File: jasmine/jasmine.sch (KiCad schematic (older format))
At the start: 74 parts, among them J1 NEIGHBOR1, J2 NEIGHBOR2, J3 USB-MICRO-B-SHIELDED, J4 LIPO_BATT_CONN, J5 2PIN_BATT_CONN, J7 BONUS_ROW, P1 TEST_POINT, P2 TEST_POINT, P3 INPUT, P4 3.7_VDC, P5 3.7_VDC, SW1 SW_SPDT, U1 MCP73831T, U2 74HC4051, U3 74HC4051, U4 PCA9674, X1 SiT1533

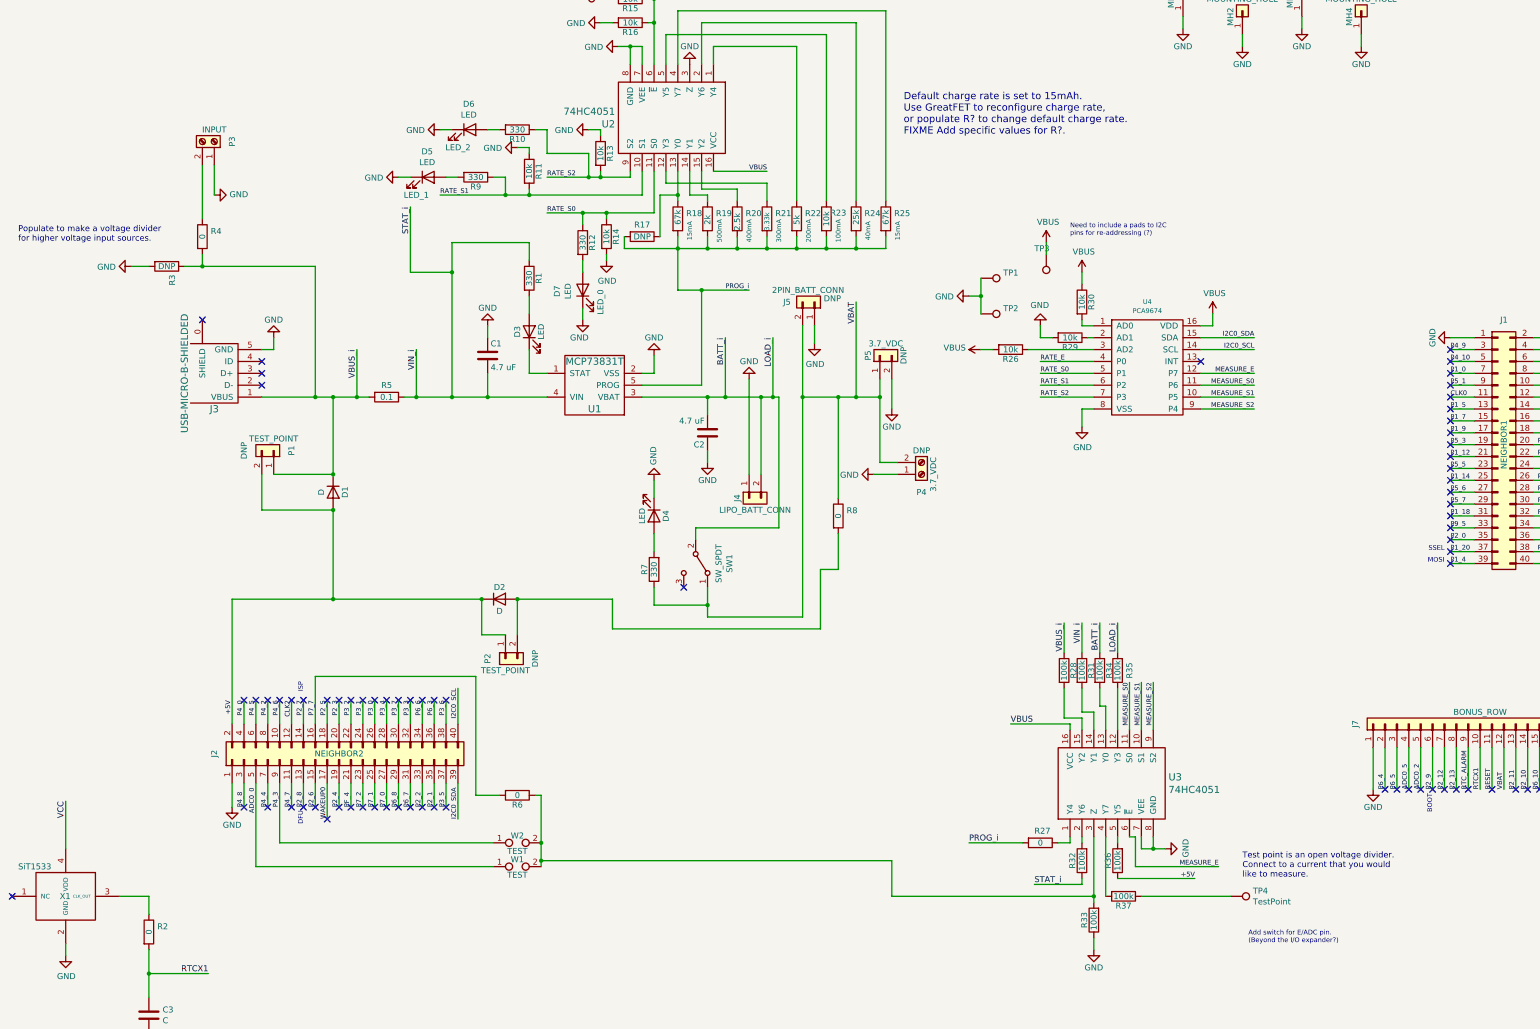
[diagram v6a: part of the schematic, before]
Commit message: Updates to jasmine schematic and layout; Updated neighbor-template to be compatible with KiCAD 5.1.2
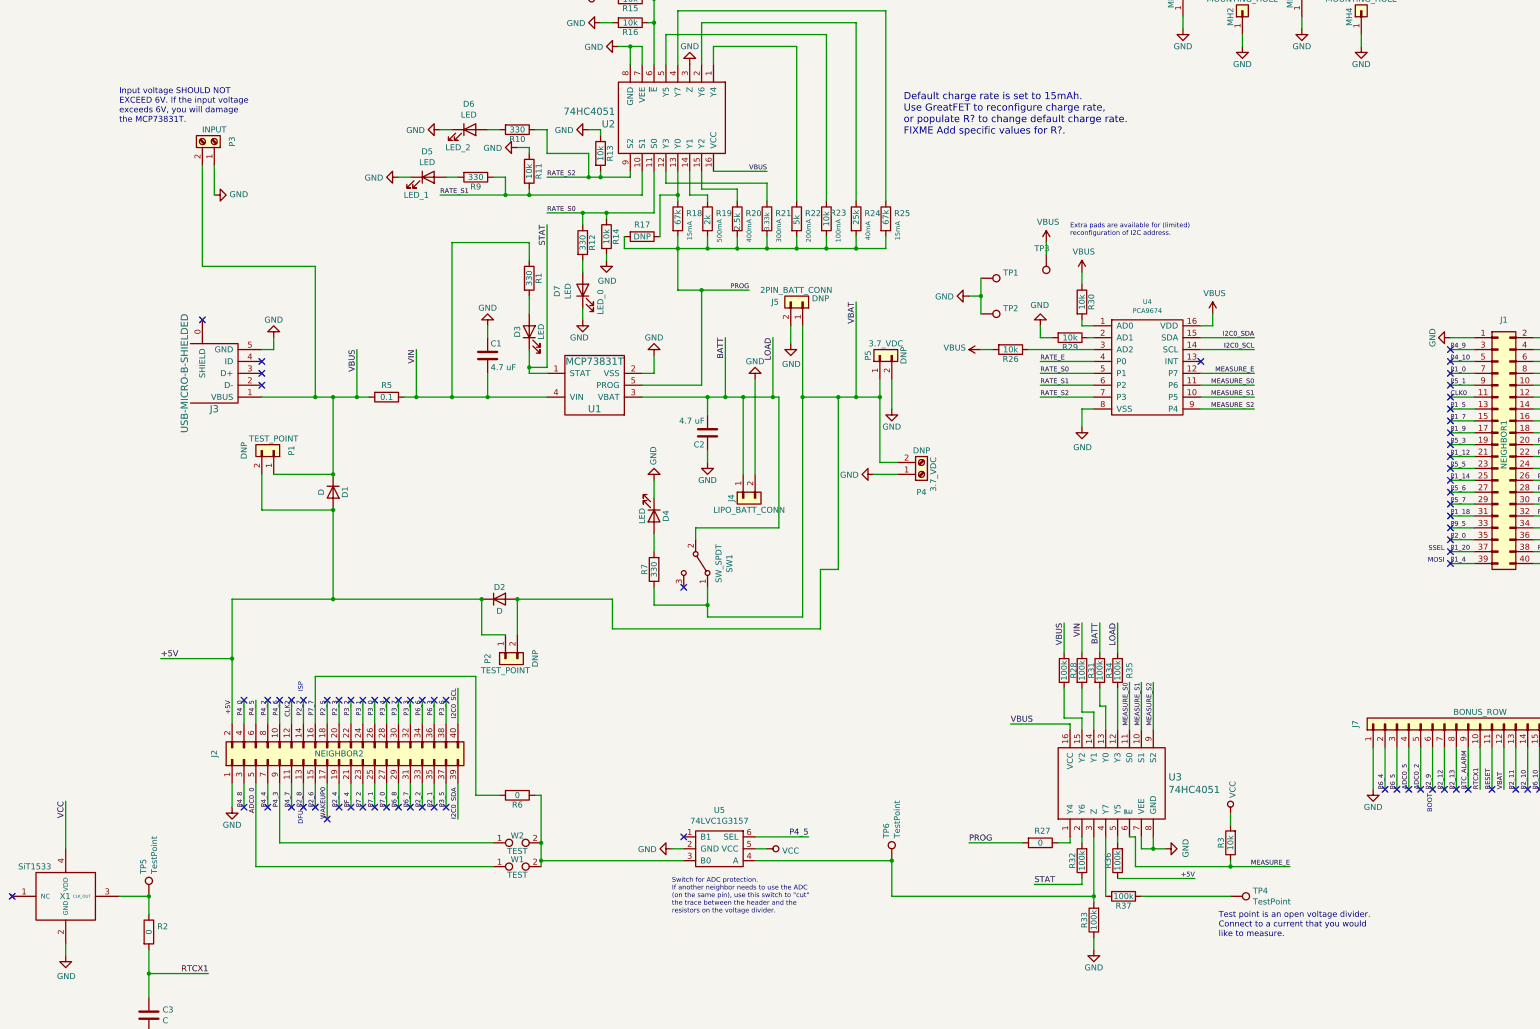
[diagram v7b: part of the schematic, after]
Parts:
- removed R4, R8: 0, gsg-modules:0603, symbol Device:R
- added TP5, TP6: TestPoint, gsg-modules:TESTPOINT-50MIL, symbol Connector:TestPoint
- added U5: 74LVC1G3157, gsg-modules:SOT363, symbol gsg-symbols:74LVC1G3157
- R3: value DNP -> 10k; Description (none) -> RES 10K OHM 1% 1/8W 0603; Manufacturer (none) -> Stackpole; Note DNP -> (none); Part Number (none) -> RNCP0603FTD10K0
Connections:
- net GND: now also J4.2 (Pin_2), J5.2 (Pin_2), U5.2 (GND); no longer J4.1 (Pin_1), J5.1 (Pin_1), R3.2
- net MEASURE_E: now also R3.1
- net P4_5: now also U5.6 (SEL)
- net VBAT: now also D2.2 (A), J5.1 (Pin_1), P2.2 (Pin_2); no longer J5.2 (Pin_2)
- net VBUS: now also D1.1 (K), J3.1 (VBUS), P1.1 (Pin_1), P3.2 (Pin_2), R28.1, R5.2
- net VCC: now also R3.2, U5.5 (VCC)
- net STAT: now reaches D3.1 (K), U1.1 (STAT)
- net STAT: now also R32.1
- net at R6.1, W1.2, W2.2: now also U5.3 (B0); no longer R33.2, U3.3 (Z)
- net at R2.1, X1.3 (CLK_OUT): now also TP5.1
- net BATT_i renamed BATT
- net BATT: now also J4.1 (Pin_1); no longer J4.2 (Pin_2)
- net PROG_i renamed PROG
- net STAT_i renamed VIN
- net VIN: no longer R32.1
- removed net VBUS_i: D1.1 (K), J3.1 (VBUS), P1.1 (Pin_1), R28.1, R3.1, R5.2
- new net: R33.2, TP6.1, U3.3 (Z), U5.4 (A)
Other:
- note added: "Extra pads are available for (limited)\nreconfiguration of I2C address."
- note added: "Input voltage SHOULD NOT\nEXCEED 6V. If the input voltage\nexceeds 6V, you will damage\nthe MCP73831T."
- note added: "Switch for ADC protection.\nIf another neighbor needs to use the ADC\n(on the same pin), use this switch to "cut"\nthe trace between the header and the\nresistors on the voltage divider."
- note removed: "Add switch for E/ADC pin.\n(Beyond the I/O expander?)"
- note removed: "Need to include a pads to I2C\npins for re-addressing (?)"
- note removed: "Populate to make a voltage divider\nfor higher voltage input sources."
- moved on the sheet: J4, J5
